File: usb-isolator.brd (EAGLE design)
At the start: 100 x 80 mm, 18 parts, among them IC1 ADUM3160BRWZ

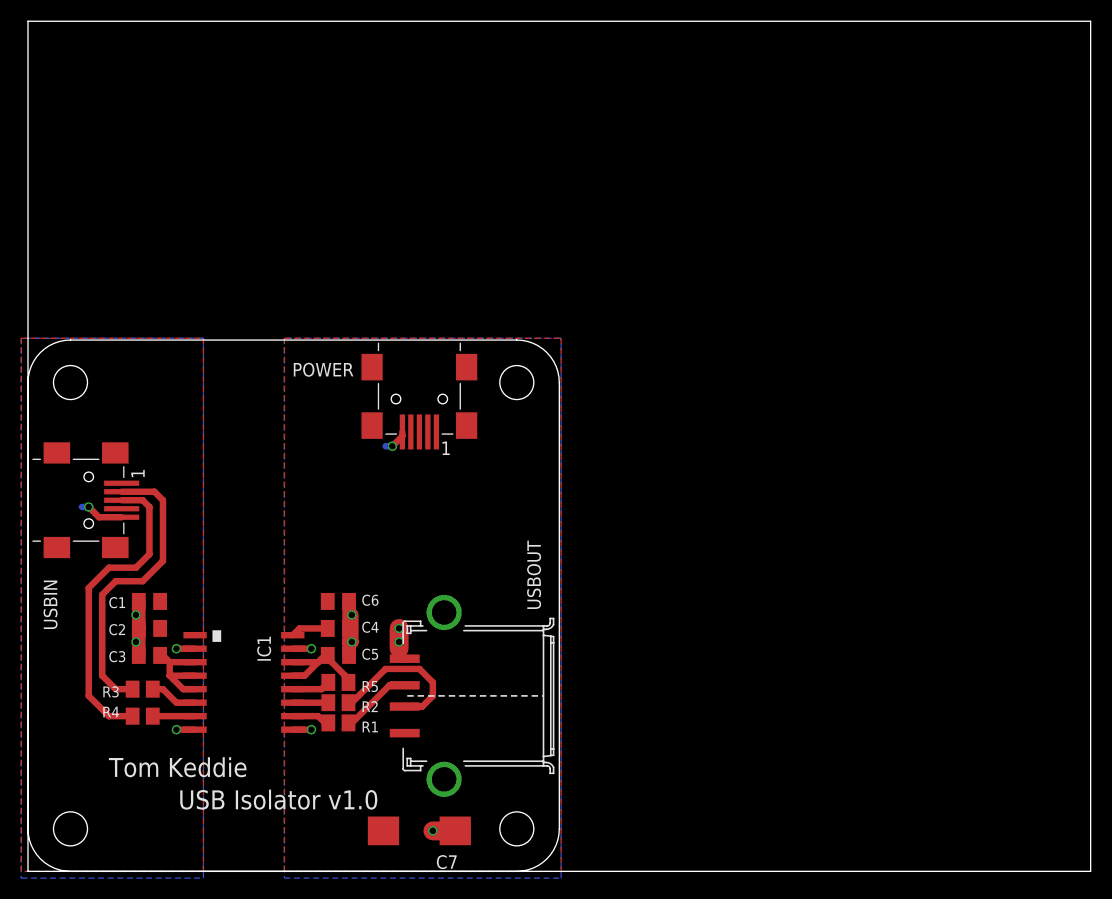
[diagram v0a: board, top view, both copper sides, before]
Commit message: Update README, eagle files and schematic image for rev 1.2
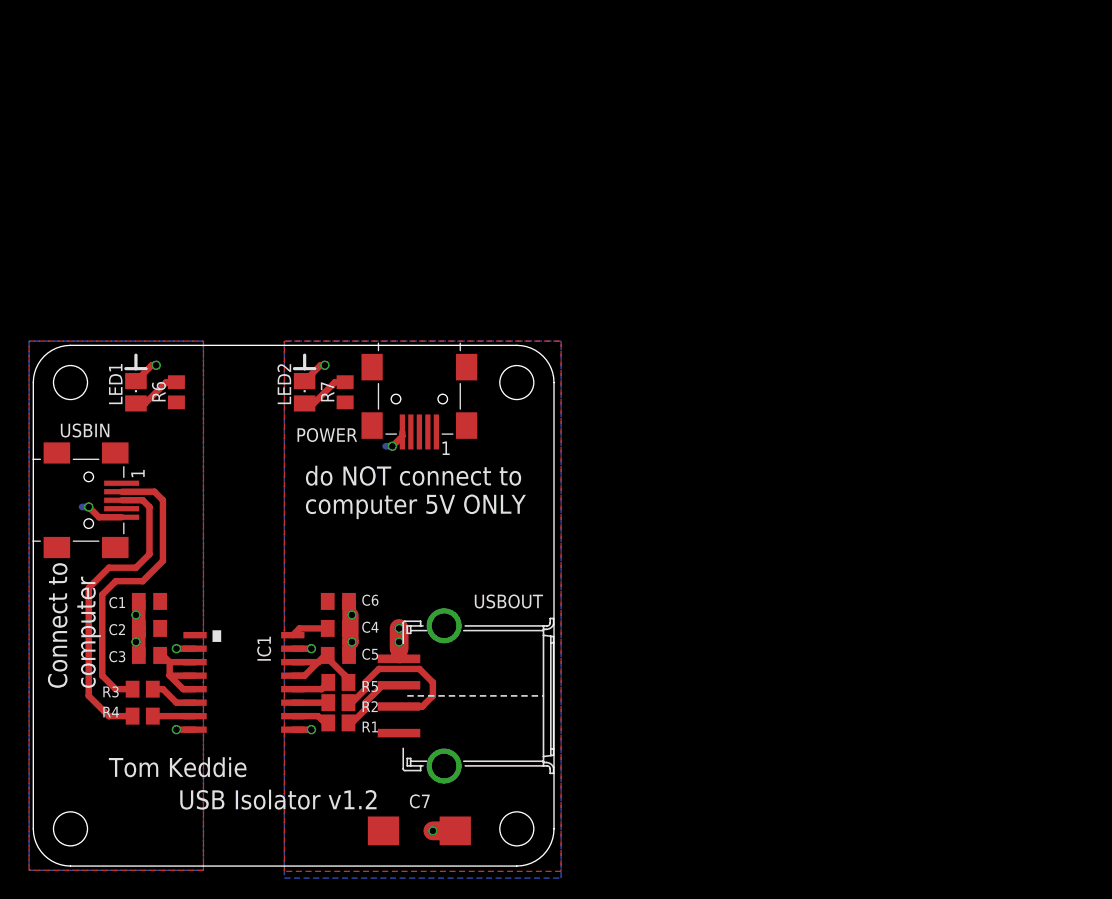
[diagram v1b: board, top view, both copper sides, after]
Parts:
- added LED1, LED2: (no value), semiconductors:LED-805
- added R6, R7: 1K, resistor:M0805
- USB-ISOLATOR: device dp_pcb:DP5050_V1 -> mechanical:DP5050_V1
- USBOUT: device dp_devices:CONN_USB_A_F -> mechanical:CONN_USB_A_F
- moved U$1 5.12 mm to (24.8, 24.1), turned to 90 degrees
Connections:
- new net N$12: LED1.A, R6.2
- new net N$13: LED2.A, R7.2
- net GND1: now also LED1.C
- net GND2: now also LED2.C
- net VBUS1: now also R6.1
- net VBUS2: now also R7.1
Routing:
- net N$12: track 0.00 -> 4.64 mm
- net N$13: track 0.00 -> 4.64 mm
- net GND1: track 13.6 -> 16.1 mm, vias 5 -> 6
- net GND2: track 19.0 -> 21.2 mm, vias 8 -> 9
- net N$8: track 14.1 -> 15.0 mm
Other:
- board size 100 x 80 mm -> 49 x 49 mm
- board text added: "Connect to computer"
- board text added: "USB Isolator v1.2"
- board text added: "do NOT connect to computer 5V ONLY"
- board text removed: "USB Isolator v1.0"
